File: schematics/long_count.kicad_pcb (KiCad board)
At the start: 2 copper layers, 148.6 x 59.7 mm, 118 parts, among them J1 CONN_01X06, J2 BARREL_JACK, Q1 Q_PNP_BEC, Q10 Q_PNP_BEC, Q11 Q_PNP_BEC, Q12 Q_PNP_BEC, Q13 Q_PNP_BEC, Q14 Q_PNP_BEC, Q15 Q_PNP_BEC, Q16 Q_PNP_BEC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

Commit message: Add mounting holes
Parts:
- added REF**: MountingHole_3.2mm_M3_Pad, Mounting_Holes:MountingHole_3.2mm_M3_Pad, F.Cu at (182.4, 80.7)
- added REF**: MountingHole_3.2mm_M3_Pad, Mounting_Holes:MountingHole_3.2mm_M3_Pad, F.Cu at (182.1, 30.6)
- added REF**: MountingHole_3.2mm_M3_Pad, Mounting_Holes:MountingHole_3.2mm_M3_Pad, F.Cu at (42.6, 29.9)
- added REF**: MountingHole_3.2mm_M3_Pad, Mounting_Holes:MountingHole_3.2mm_M3_Pad, F.Cu at (42.8, 80.3)
- D1: value LED -> STAT
- D2: value LED -> PWR
- J1: value CONN_01X06 -> PICKIT connector
- U2: value LM350T -> LM7805CT
- Y1: value Crystal -> 12MHz
- moved SW2 7.07 mm to (177.2, 69.5)
- moved SW3 6.21 mm to (177.2, 60.3)
- moved U2 5.40 mm to (133.1, 77.9), turned to 0 degrees
- moved SW1 4.35 mm to (177.1, 44.8)
- moved C3 4.13 mm to (133.3, 81.3)
- moved SW4 2.78 mm to (177.2, 51.3)
- moved C6 1.99 mm to (139.0, 81.3), turned to 0 degrees
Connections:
- U2 pad 1: GND -> Net-(C3-Pad2)
- U2 pad 2: +5V -> GND
- U2 pad 3: Net-(C3-Pad2) -> +5V
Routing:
- net Net-(R18-Pad1): track 74.7 -> 41.5 mm
- net Net-(R2-Pad1): track 89.2 -> 59.7 mm
- net Net-(R16-Pad2): track 58.4 -> 76.0 mm, vias 2 -> 0
- net ICSPCLK: track 92.0 -> 75.3 mm, vias 1 -> 0
- net +5V: track 165.2 -> 152.2 mm, vias 3 -> 2
- net Net-(C3-Pad2): track 29.2 -> 18.2 mm
- net Net-(R1-Pad2): track 56.3 -> 67.2 mm
- net Net-(R17-Pad1): track 43.4 -> 36.7 mm, vias 0 -> 1
- net Net-(R15-Pad2): track 54.1 -> 57.8 mm
- net Net-(R4-Pad2): track 39.1 -> 42.4 mm
- net Net-(R18-Pad2): track 28.7 -> 30.7 mm
- net Net-(R17-Pad2): track 19.6 -> 17.8 mm
- net (no net): track 1.19 -> 0.00 mm, vias 1 -> 0

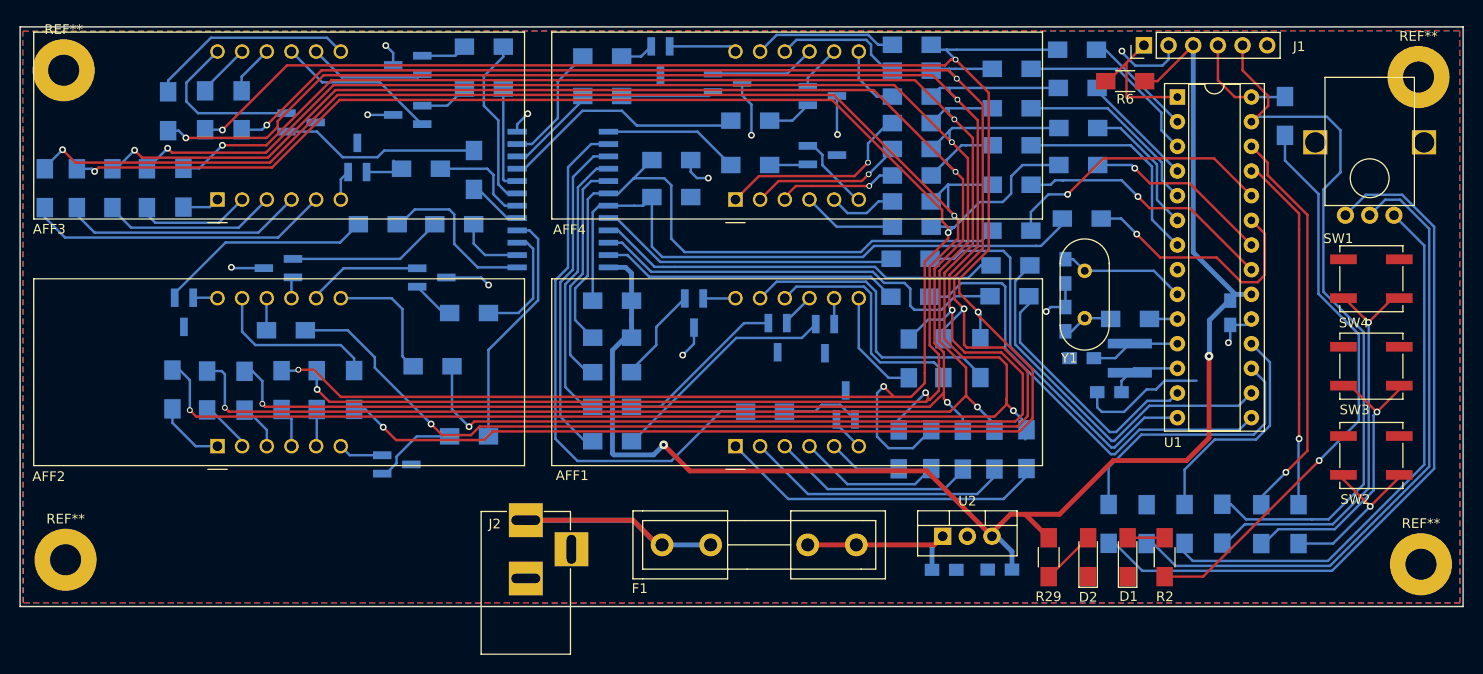
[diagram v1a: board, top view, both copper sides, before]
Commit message: Add silkscreen, move top left mounting hole so it's uncovered
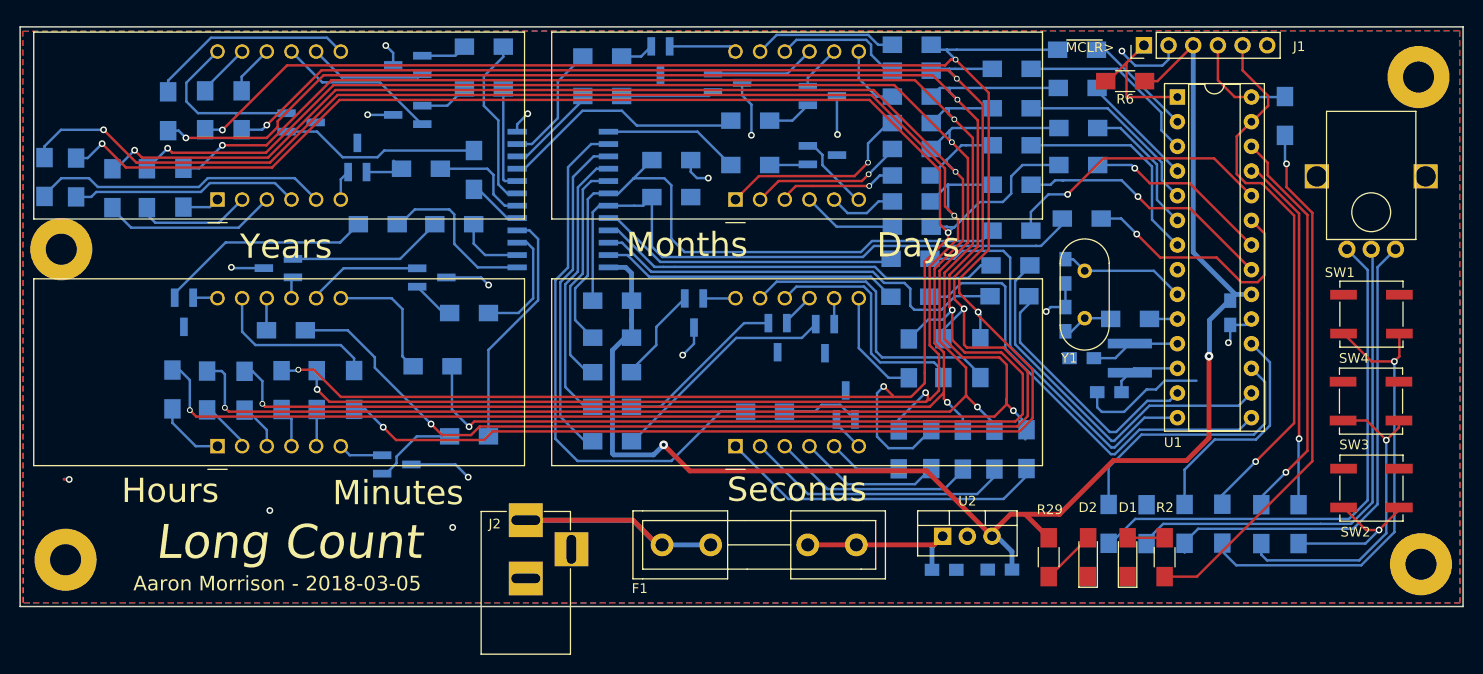
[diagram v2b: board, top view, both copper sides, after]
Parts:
- moved REF** 18.4 mm to (42.3, 48.3)
- moved SW4 3.65 mm to (177.3, 55.0)
- moved SW3 3.60 mm to (177.2, 63.9)
- moved SW1 3.50 mm to (177.2, 48.3)
- moved SW2 3.36 mm to (177.3, 72.9)
- moved R65 1.15 mm to (40.6, 40.9)
- moved R69 1.11 mm to (43.9, 40.9)
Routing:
- net Net-(R16-Pad2): track 76.0 -> 56.6 mm
- net ICSPCLK: track 75.3 -> 56.9 mm, vias 0 -> 1
- net Net-(R1-Pad2): track 67.2 -> 52.9 mm
- net Net-(R15-Pad2): track 57.8 -> 51.1 mm
- net GND: track 61.2 -> 67.6 mm, vias 12 -> 13
- net Net-(R4-Pad2): track 42.4 -> 48.2 mm
- net Net-(R2-Pad1): track 59.7 -> 55.3 mm
- net SEG_G: track 206.8 -> 210.9 mm
- net SEG_C: track 215.8 -> 219.5 mm
- net Net-(R18-Pad2): track 30.7 -> 33.5 mm
- net Net-(AFF3-Pad4): track 25.0 -> 23.5 mm
- net Net-(R17-Pad2): track 17.8 -> 16.7 mm
- net (no net): track 0.00 -> 1.10 mm, vias 0 -> 3
- net Net-(AFF3-Pad5): track 31.4 -> 30.5 mm
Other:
- board text added: "Aaron Morrison - 2018-03-05"
- board text added: "Days"
- board text added: "Hours"
- board text added: "Long Count"
- board text added: "Minutes"
- board text added: "Months"
- board text added: "Seconds"
- board text added: "Years"
- board text added: "~MCLR~>"
